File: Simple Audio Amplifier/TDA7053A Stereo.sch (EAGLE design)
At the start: 23 parts, among them IC1 TDA7052A

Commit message: Simple Audio Amp
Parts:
- removed C3: 2u2, SparkFun:CAP_POLPTH1
- removed C4: 1u, SparkFun:CAPPTH2
- removed IC1: TDA7052A, My Library:TDA7052A
- removed JP1, JP3, JP4: (no value), pinhead:PINHD-1X2
- removed JP2: (no value), pinhead:PINHD-1X4
- removed R2: 1k, adafruit:R-US_0204/5
- removed R5: 56k, adafruit:R-US_0204/5
- removed SP1: SP, My Library:SP
- removed TRIM: 25k, adafruit:TRIMPOTTC33X
- removed VR: 1M, My Library:POT-RV16AF-20
- added J1: POWER_JACKSLT, SparkFun:POWER_JACKSLT
- added U1: (no value), SparkFun:AUDIO-JACKPTH
- C1: value 220u -> 0.1u; device SparkFun:CAP_POLPTH1 -> SparkFun:CAPPTH2
- C2: value 0.1u -> 220u; device SparkFun:CAPPTH2 -> SparkFun:CAP_POLPTH1
- VR1: value 22k -> 1M
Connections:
- removed net AGND: C1.-, C2.2, C4.2, IC1.GND1, IC1.GND2, JP3.2, JP4.2, R2.1, VR.A
- removed net IN: C3.+, JP3.1
- removed net N$1: C1.+, C2.1, IC1.VP, JP4.1
- removed net N$13: C3.-, TRIM.E
- removed net N$16: C8.1, R5.1, VR1.E
- removed net N$2: IC1.IN+, TRIM.S
- removed net N$3: R2.2, TRIM.A
- removed net N$5: C4.1, IC1.VC, VR.E, VR.S
- removed net N$8: IC1.OUT-, SP1.+
- removed net N$9: IC1.OUT+, SP1.-
- net GND: now also C1.2, C2.-, J1.GND, U1.SLEEVE; no longer JP1.2, JP2.3, JP2.4
- net N$17: now also C1.1, C2.+, J1.PWR; no longer JP1.1, R5.2
- net N$19: now also C8.1, VR1.E
- net N$4: now also U1.RIGHT; no longer JP2.1
- net N$6: now also U1.LEFT; no longer JP2.2
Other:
- moved on the sheet: C5, C6, C8, R1, R3, U$1, VR1

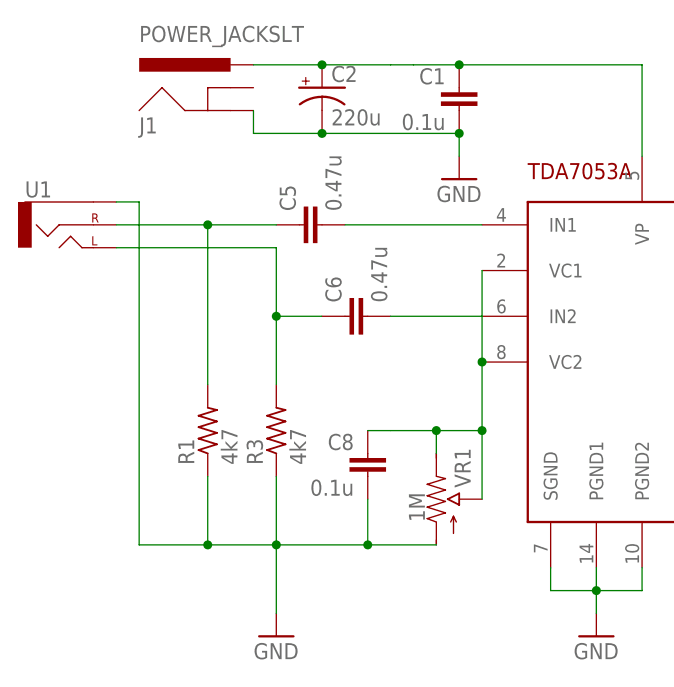
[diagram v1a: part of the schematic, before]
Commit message: TDA7053 Stereo Audio Power Amplifier
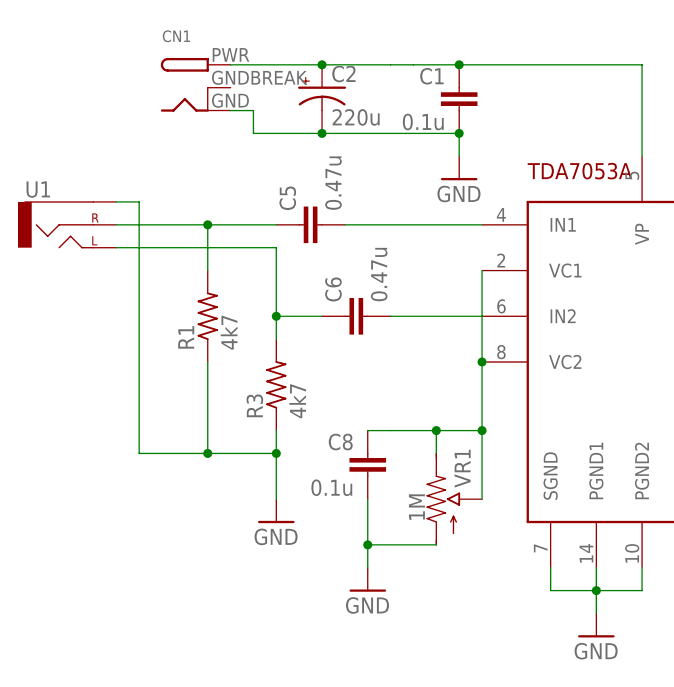
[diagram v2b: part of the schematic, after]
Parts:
- removed J1: POWER_JACKSLT, SparkFun:POWER_JACKSLT
- added CN1: (no value), adafruit:DCBARRELPTH
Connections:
- net GND: now also CN1.GND; no longer J1.GND
- net N$17: now also CN1.PWR; no longer J1.PWR
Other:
- moved on the sheet: R1, R3
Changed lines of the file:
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@@
 <part name="C8" library="SparkFun" deviceset="CAP" device="PTH2" value="0.1u"/>
 <part name="U1" library="SparkFun" deviceset="AUDIO-JACK" device="PTH"/>
-<part name="J1" library="SparkFun" deviceset="POWER_JACK" device="SLT"/>
 <part name="C1" library="SparkFun" deviceset="CAP" device="PTH2" value="0.1u"/>
 <part name="C2" library="SparkFun" deviceset="CAP_POL" device="PTH1" value="220u"/>
+<part name="GND2" library="SparkFun" deviceset="GND" device=""/>
+<part name="CN1" library="adafruit" deviceset="DCBARREL" device="PTH"/>
 </parts>
 <sheets>
@@
 </plain>
 <instances>
-<instance part="R1" gate="G$1" x="50.8" y="81.28" rot="R90"/>
-<instance part="R3" gate="G$1" x="58.42" y="81.28" rot="R90"/>
+<instance part="R1" gate="G$1" x="50.8" y="93.98" rot="R90"/>
+<instance part="R3" gate="G$1" x="58.42" y="86.36" rot="R90"/>
 <instance part="GND6" gate="1" x="93.98" y="58.42"/>
 <instance part="SP2" gate="S1" x="129.54" y="99.06" rot="R270"/>
@@
 <instance part="GND7" gate="1" x="78.74" y="109.22"/>
 <instance part="U$1" gate="G$1" x="99.06" y="88.9"/>
-<instance part="GND1" gate="1" x="58.42" y="58.42"/>
+<instance part="GND1" gate="1" x="58.42" y="71.12"/>
 <instance part="C5" gate="G$1" x="63.5" y="104.14" rot="R90"/>
 <instance part="C6" gate="G$1" x="68.58" y="93.98" rot="R90"/>
@@
 <instance part="C8" gate="G$1" x="68.58" y="76.2" rot="MR0"/>
 <instance part="U1" gate="G$1" x="35.56" y="104.14"/>
-<instance part="J1" gate="G$1" x="53.34" y="114.3"/>
 <instance part="C1" gate="G$1" x="78.74" y="116.84" rot="MR0"/>
 <instance part="C2" gate="G$1" x="63.5" y="119.38"/>
+<instance part="GND2" gate="1" x="68.58" y="63.5"/>
+<instance part="CN1" gate="G$1" x="50.8" y="119.38"/>
 </instances>
 <busses>
@@
 <net name="GND" class="0">
 <segment>
-<wire x1="55.88" y1="116.84" x2="55.88" y2="114.3" width="0.1524" layer="91"/>
 <pinref part="GND7" gate="1" pin="GND"/>
-<wire x1="55.88" y1="114.3" x2="63.5" y2="114.3" width="0.1524" layer="91"/>
-<pinref part="J1" gate="G$1" pin="GND"/>
 <pinref part="C1" gate="G$1" pin="2"/>
 <pinref part="C2" gate="G$1" pin="-"/>
 <wire x1="63.5" y1="114.3" x2="78.74" y2="114.3" width="0.1524" layer="91"/>
-<junction x="63.5" y="114.3"/>
 <wire x1="78.74" y1="111.76" x2="78.74" y2="114.3" width="0.1524" layer="91"/>
 <junction x="78.74" y="114.3"/>
+<wire x1="55.88" y1="116.84" x2="55.88" y2="114.3" width="0.1524" layer="91"/>
+<wire x1="55.88" y1="114.3" x2="63.5" y2="114.3" width="0.1524" layer="91"/>
+<junction x="63.5" y="114.3"/>
+<wire x1="53.34" y1="116.84" x2="55.88" y2="116.84" width="0.1524" layer="91"/>
+<pinref part="CN1" gate="G$1" pin="GND"/>
 </segment>
 <segment>
-<wire x1="58.42" y1="68.58" x2="50.8" y2="68.58" width="0.1524" layer="91"/>
-<wire x1="50.8" y1="68.58" x2="43.18" y2="68.58" width="0.1524" layer="91"/>
+<pinref part="GND2" gate="1" pin="GND"/>
+<pinref part="C8" gate="G$1" pin="2"/>
+<wire x1="68.58" y1="73.66" x2="68.58" y2="68.58" width="0.1524" layer="91"/>
+<pinref part="VR1" gate="G$1" pin="A"/>
+<wire x1="76.2" y1="68.58" x2="68.58" y2="68.58" width="0.1524" layer="91"/>
+<junction x="68.58" y="68.58"/>
+<wire x1="68.58" y1="68.58" x2="68.58" y2="66.04" width="0.1524" layer="91"/>
+</segment>
+<segment>
+<wire x1="58.42" y1="78.74" x2="50.8" y2="78.74" width="0.1524" layer="91"/>
+<wire x1="50.8" y1="78.74" x2="43.18" y2="78.74" width="0.1524" layer="91"/>
 <pinref part="R3" gate="G$1" pin="1"/>
 <pinref part="R1" gate="G$1" pin="1"/>
-<wire x1="50.8" y1="76.2" x2="50.8" y2="68.58" width="0.1524" layer="91"/>
-<junction x="50.8" y="68.58"/>
+<wire x1="50.8" y1="88.9" x2="50.8" y2="78.74" width="0.1524" layer="91"/>
+<junction x="50.8" y="78.74"/>
 <wire x1="40.64" y1="106.68" x2="43.18" y2="106.68" width="0.1524" layer="91"/>
-<wire x1="43.18" y1="106.68" x2="43.18" y2="68.58" width="0.1524" layer="91"/>
+<wire x1="43.18" y1="106.68" x2="43.18" y2="78.74" width="0.1524" layer="91"/>
 <pinref part="GND1" gate="1" pin="GND"/>
-<wire x1="58.42" y1="76.2" x2="58.42" y2="68.58" width="0.1524" layer="91"/>
-<pinref part="C8" gate="G$1" pin="2"/>
-<wire x1="58.42" y1="68.58" x2="58.42" y2="60.96" width="0.1524" layer="91"/>
-<wire x1="68.58" y1="73.66" x2="68.58" y2="68.58" width="0.1524" layer="91"/>
-<wire x1="76.2" y1="68.58" x2="68.58" y2="68.58" width="0.1524" layer="91"/>
-<pinref part="VR1" gate="G$1" pin="A"/>
-<wire x1="58.42" y1="68.58" x2="68.58" y2="68.58" width="0.1524" layer="91"/>
-<junction x="68.58" y="68.58"/>
-<junction x="58.42" y="68.58"/>
+<wire x1="58.42" y1="81.28" x2="58.42" y2="78.74" width="0.1524" layer="91"/>
+<wire x1="58.42" y1="78.74" x2="58.42" y2="73.66" width="0.1524" layer="91"/>
+<junction x="58.42" y="78.74"/>
 <pinref part="U1" gate="G$1" pin="SLEEVE"/>
 </segment>
@@
 <pinref part="C5" gate="G$1" pin="1"/>
 <pinref part="R1" gate="G$1" pin="2"/>
-<wire x1="50.8" y1="86.36" x2="50.8" y2="104.14" width="0.1524" layer="91"/>
+<wire x1="50.8" y1="99.06" x2="50.8" y2="104.14" width="0.1524" layer="91"/>
 <wire x1="50.8" y1="104.14" x2="58.42" y2="104.14" width="0.1524" layer="91"/>
 <wire x1="43.18" y1="104.14" x2="40.64" y2="104.14" width="0.1524" layer="91"/>
@@
 <pinref part="C6" gate="G$1" pin="1"/>
 <wire x1="63.5" y1="93.98" x2="58.42" y2="93.98" width="0.1524" layer="91"/>
-<wire x1="58.42" y1="93.98" x2="58.42" y2="86.36" width="0.1524" layer="91"/>
+<wire x1="58.42" y1="93.98" x2="58.42" y2="91.44" width="0.1524" layer="91"/>
 <wire x1="40.64" y1="101.6" x2="58.42" y2="101.6" width="0.1524" layer="91"/>
 <wire x1="58.42" y1="101.6" x2="58.42" y2="93.98" width="0.1524" layer="91"/>
@@
 <net name="N$17" class="0">
 <segment>
-<wire x1="55.88" y1="121.92" x2="63.5" y2="121.92" width="0.1524" layer="91"/>
+<wire x1="53.34" y1="121.92" x2="63.5" y2="121.92" width="0.1524" layer="91"/>
 <wire x1="63.5" y1="121.92" x2="71.12" y2="121.92" width="0.1524" layer="91"/>
 <wire x1="71.12" y1="121.92" x2="73.66" y2="121.92" width="0.1524" layer="91"/>
@@
 <wire x1="99.06" y1="121.92" x2="99.06" y2="111.76" width="0.1524" layer="91"/>
 <pinref part="U$1" gate="G$1" pin="VP"/>
-<pinref part="J1" gate="G$1" pin="PWR"/>
 <pinref part="C1" gate="G$1" pin="1"/>
 <junction x="78.74" y="121.92"/>
 <pinref part="C2" gate="G$1" pin="+"/>
 <junction x="63.5" y="121.92"/>
+<pinref part="CN1" gate="G$1" pin="PWR"/>
 </segment>
 </net>
